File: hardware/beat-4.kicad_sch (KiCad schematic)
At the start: 36 parts, among them J101 Cortex, J102 DX07S016JA3, SW101 SKSG, SW102 SKSG, U101 ATSAMD51G, U102 TPS78433QWDRBRQ1, Y101 32k768

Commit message: Rename
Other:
- sheet PowerDelivery renamed Power USB
- sheet MIDI In: file MIDIIn.kicad_sch -> MIDI-In.kicad_sch
- sheet Power +5V: file PowerSupply.kicad_sch -> Power-DCDC.kicad_sch
- sheet Power USB: file PowerDelivery.kicad_sch -> Power-USB.kicad_sch

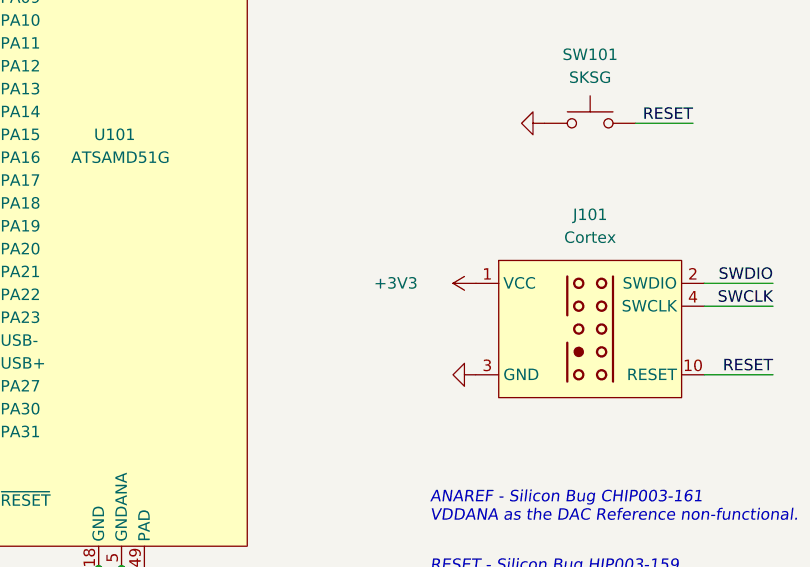
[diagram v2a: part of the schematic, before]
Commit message: Update USB-PD SWD
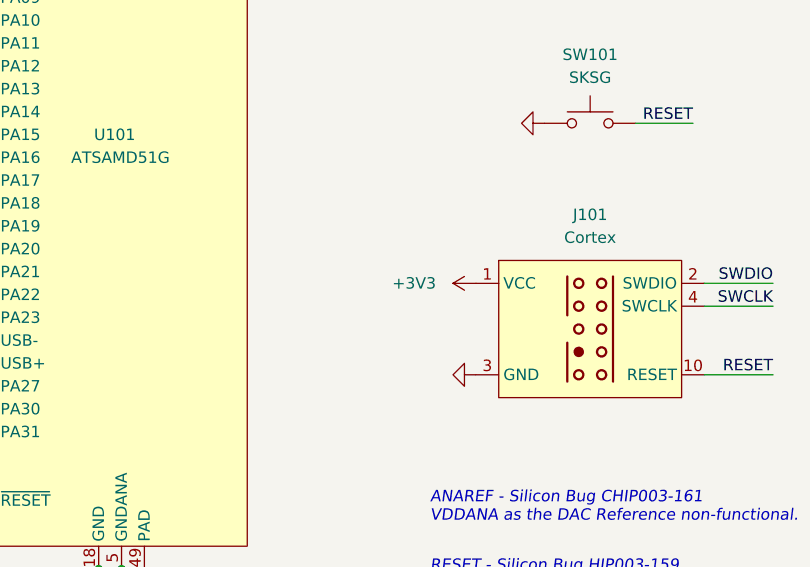
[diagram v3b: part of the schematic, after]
